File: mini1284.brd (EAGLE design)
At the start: 69.8 x 20.8 mm, 37 parts, among them U1 ATMEGA644A

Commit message: Routing looking pretty good.
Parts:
- removed C10, C11, C12, R10, R2, R3, R4, R5, R6, R7, R8, R9: (no value), _jc:M0805
- removed C13: 100nF, _jc:M0805
- removed D2: (no value), _jc:CHIPLED_1206
- removed D3: 1N4148, _jc:SOD-323F
- removed R11: 10K, _jc:M0805
- added LOGO2: OSHW_LOGO_6MILX0100-NT, ohw-logo:OSHW_6X100_NOTEXT
- C1, C2, C3, C4, C5, C9: value (none) -> 100nF
- C6: value (none) -> 10uF; device _jc:M0805 -> _jc:M1206
- C7, C8: value (none) -> 27pF
- D1: value (none) -> 1N4148; device _jc:SOD-323F -> _jc:SOD-323F-A
- L1: value (none) -> 10uH
- R1: value (none) -> 10K
- S1: device _jc:B3F-10XXOCT -> _jc:PTS810
- Y1: value (none) -> 16MHz
- moved D1 189.3 mm to (52.7, 14.3)
- moved R1 133.1 mm to (52.8, 12.1)
- moved C9 113.0 mm to (58.3, 8.10), turned to 270 degrees
- moved C7 40.9 mm to (11.3, 11.9)
- moved C8 34.7 mm to (11.3, 6.50)
- moved C6 28.2 mm to (46.8, 8.26)
- moved C5 21.8 mm to (40.4, 12.3)
- moved S1 6.08 mm to (52.9, 7.70), turned to 180 degrees
- moved C4 5.08 mm to (40.4, 7.62)
- moved JP6 5.08 mm to (62.2, 16.5)
- moved C1 5.08 mm to (19.3, 14.1)
- moved JP3 5.08 mm to (38.1, 1.27)
- moved JP4 5.08 mm to (38.1, 19.1)
- moved L1 5.08 mm to (43.2, 7.62)
- moved U1 4.45 mm to (30.5, 10.1)
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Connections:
- net /RESET: now also C9.1, D1.A, R1.1, S1.3, S1.4; no longer C13.1, D3.A, R11.1, S1.1, S1.2
- net AREF: now also C5.1; no longer C8.1
- net GND: now also S1.1, S1.2; no longer S1.3, S1.4
- net N$2: now also C8.1; no longer C6.1
- net N$3: now also C7.1; no longer C5.1
- net RST: now also C9.2; no longer C13.2
- net VCC: now also C6.1, D1.K, R1.2; no longer C7.1, D3.K, R11.2
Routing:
- net /RESET: track 99.2 -> 77.0 mm
- net VCC: track 112.8 -> 100.0 mm, vias 2 -> 1
- net N$14: track 20.6 -> 15.8 mm
- net SCK: track 37.6 -> 32.9 mm
- net N$11: track 17.4 -> 12.7 mm
- net N$9: track 20.6 -> 16.0 mm
- net N$16: track 17.3 -> 12.7 mm
- net N$15: track 20.8 -> 16.3 mm
- net N$17: track 17.5 -> 13.0 mm
- net MOSI: track 31.6 -> 27.1 mm
- net N$7: track 21.0 -> 16.5 mm
- net MISO: track 31.8 -> 27.4 mm
- net N$13: track 20.3 -> 15.9 mm
- net N$10: track 20.7 -> 16.4 mm
- net N$8: track 20.1 -> 15.9 mm
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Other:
- board size 69.8 x 20.8 mm -> 64.8 x 20.8 mm
- board text added: "0"
- board text added: "1"
- board text added: "10"
- board text added: "11"
- board text added: "12"
- board text added: "13"
- board text added: "14"
- board text added: "15"
- board text added: "16"
- board text added: "17"
- board text added: "18"
- board text added: "19"
- board text added: "2"
- board text added: "20"
- board text added: "21"
- board text added: "22"
- board text added: "23"
- board text added: "3"
- board text added: "4"
- board text added: "5"
- board text added: "6"
- board text added: "7"
- board text added: "8"
- board text added: "9"
- board text added: "A0"
- board text added: "A1"
- board text added: "A2"
- board text added: "A3"
- board text added: "A4"
- board text added: "A5"
- board text added: "A6"
- board text added: "A7"
- board text added: "BLK"
- board text added: "FTDI"
- board text added: "GRN"
- board text added: "ICSP"
- board text added: "RESET"
- board text added: "VCC"
- board text removed: "Vcc"

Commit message: Routing refinements.
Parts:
- added D2: LED, _jc:D0805A
- added LOGO1: OSHW_LOGO_8MILX0150-NT, ohw-logo:OSHW_8X150_NOTEXT
- added R2: 1K, _jc:M0805
- moved JP5 1.93 mm to (3.05, 14.5)
- moved C8 1.82 mm to (12.3, 8.03)
- moved Y1 1.44 mm to (16.0, 10.2)
- moved C7 1.08 mm to (12.3, 12.2)
- moved C1 0.51 mm to (19.8, 14.1)
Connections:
- new net N$34: D2.K, R2.2
- net GND: now also R2.1
- net SCK: now also D2.A
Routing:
- net SCK: track 32.9 -> 39.1 mm
- net N$34: track 0.00 -> 2.42 mm
- net N$3: track 18.0 -> 16.6 mm
- net N$2: track 15.0 -> 13.5 mm
- net MISO: track 27.4 -> 25.9 mm
- net MOSI: track 27.1 -> 25.8 mm
- net VCC: track 100.0 -> 101.1 mm
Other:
- board text added: "CC BY-SA"
- board text added: "Mighty Mini 1284P"
- board text added: "jc 0414 v1.0"
- board text added: "open"
- board text added: "source"

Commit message: Further tweaks.
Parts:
- U1: value ATMEGA644A -> ATmega1284P-AU
- moved LOGO1 1.27 mm to (16.1, 9.73)
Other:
- board text added: "goo.gl/5fAHca"
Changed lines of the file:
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@@
 <layer number="20" name="Dimension" color="15" fill="1" visible="yes" active="yes"/>
 <layer number="21" name="tPlace" color="7" fill="1" visible="yes" active="yes"/>
-<layer number="22" name="bPlace" color="7" fill="1" visible="yes" active="yes"/>
+<layer number="22" name="bPlace" color="7" fill="1" visible="no" active="yes"/>
 <layer number="23" name="tOrigins" color="15" fill="1" visible="yes" active="yes"/>
 <layer number="24" name="bOrigins" color="15" fill="1" visible="no" active="yes"/>
@@
 <text x="59.69" y="10.16" size="1.27" layer="22" ratio="16" rot="MR0">CC BY-SA</text>
 <text x="59.69" y="7.62" size="1.27" layer="22" ratio="16" rot="MR0">jc 0414 v1.0</text>
-<text x="13.97" y="13.716" size="1.27" layer="22" ratio="16" rot="MR0" align="center">open</text>
-<text x="13.97" y="7.366" size="1.27" layer="22" ratio="16" rot="MR0" align="center">source</text>
+<text x="13.97" y="14.986" size="1.27" layer="22" ratio="16" rot="MR0" align="center">open</text>
+<text x="13.97" y="8.636" size="1.27" layer="22" ratio="16" rot="MR0" align="center">source</text>
+<text x="13.97" y="6.096" size="1.27" layer="22" ratio="16" rot="MR0" align="center">goo.gl/5fAHca</text>
 </plain>
 <attributes>
@@
 </autorouter>
 <elements>
-<element name="U1" library="atmel" package="TQFP44" value="ATMEGA644A" x="30.48" y="10.1346" smashed="yes">
+<element name="U1" library="atmel" package="TQFP44" value="ATmega1284P-AU" x="30.48" y="10.1346" smashed="yes">
 <attribute name="OC_NEWARK" value="58M3748" x="57.149990625" y="-0.0254" size="1.778" layer="27" display="off"/>
 <attribute name="MPN" value="ATMEGA644PV-10AU" x="57.149990625" y="-0.0254" size="1.778" layer="27" display="off"/>
@@
 </element>
 <element name="LOGO2" library="ohw-logo" package="OSHW_6X100_NOTEXT" value="OSHW_LOGO_6MILX0100-NT" x="42.926" y="12.446"/>
-<element name="LOGO1" library="ohw-logo" package="OSHW_8X150_NOTEXT" value="OSHW_LOGO_8MILX0150-NT" x="16.1036" y="8.4582" rot="MR0"/>
+<element name="LOGO1" library="ohw-logo" package="OSHW_8X150_NOTEXT" value="OSHW_LOGO_8MILX0150-NT" x="16.1036" y="9.7282" rot="MR0"/>
 <element name="R2" library="_jc" package="M0805" value="1K" x="8.128" y="5.334" smashed="yes" rot="R180">
 <attribute name="NAME" x="6.374" y="6.834" size="0.8128" layer="25" ratio="16"/>

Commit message: First run sent to fab.
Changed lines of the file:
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@@
 <setting verticaltext="up"/>
 </settings>
-<grid distance="0.05" unitdist="inch" unit="inch" style="dots" multiple="1" display="yes" altdistance="0.001" altunitdist="inch" altunit="inch"/>
+<grid distance="0.05" unitdist="inch" unit="inch" style="dots" multiple="1" display="yes" altdistance="0.01" altunitdist="inch" altunit="inch"/>
 <layers>
 <layer number="1" name="Top" color="4" fill="1" visible="yes" active="yes"/>
@@
 <wire x1="1.27" y1="20.574" x2="0" y2="19.304" width="0" layer="20" curve="90"/>
 <text x="2.54" y="3.302" size="1.016" layer="21" ratio="16" rot="R180" align="center">RST</text>
-<text x="24.638" y="18.796" size="0.8128" layer="21" ratio="16">PB7:0</text>
-<text x="24.638" y="0.508" size="0.8128" layer="21" ratio="16">PD0:7</text>
-<text x="33.02" y="18.796" size="0.8128" layer="21" ratio="16">PA0:7</text>
-<text x="33.274" y="0.508" size="0.8128" layer="21" ratio="16">PC0:7</text>
+<text x="24.384" y="17.526" size="0.8128" layer="21" ratio="16">PB7:0</text>
+<text x="24.384" y="2.286" size="0.8128" layer="21" ratio="16">PD0:7</text>
+<text x="33.274" y="17.526" size="0.8128" layer="21" ratio="16">PA0:7</text>
+<text x="33.528" y="2.286" size="0.8128" layer="21" ratio="16">PC0:7</text>
 <text x="52.9082" y="5.1816" size="1.016" layer="21" ratio="16" align="center">RESET</text>
 <text x="22.86" y="17.018" size="1.016" layer="21" ratio="16" align="center">0</text>
@@
 </element>
 <element name="C1" library="_jc" package="M0805" value="100nF" x="19.812" y="14.0716" smashed="yes" rot="R90">
-<attribute name="NAME" x="18.2358" y="14.0956" size="0.8128" layer="25" ratio="16" rot="R90"/>
+<attribute name="NAME" x="21.487" y="10.5396" size="0.8128" layer="25" ratio="16" rot="R90"/>
 <attribute name="VALUE" x="22.312" y="12.5716" size="0.8128" layer="27" ratio="16" rot="R90"/>
 </element>
 <element name="C2" library="_jc" package="M0805" value="100nF" x="30.2514" y="1.4732" smashed="yes" rot="R180">
-<attribute name="NAME" x="26.6686" y="2.4398" size="0.8128" layer="25" ratio="16"/>
+<attribute name="NAME" x="33.3742" y="0.2526" size="0.8128" layer="25" ratio="16" rot="R90"/>
 <attribute name="VALUE" x="31.7514" y="3.9732" size="0.8128" layer="27" ratio="16" rot="R180"/>
 </element>
 <element name="C3" library="_jc" package="M0805" value="100nF" x="30.5308" y="18.923" smashed="yes" rot="R180">
-<attribute name="NAME" x="26.7956" y="17.248" size="0.8128" layer="25" ratio="16"/>
+<attribute name="NAME" x="28.218" y="18.9216" size="0.8128" layer="25" ratio="16" rot="R90"/>
 <attribute name="VALUE" x="32.0308" y="21.423" size="0.8128" layer="27" ratio="16" rot="R180"/>
 </element>
@@
 <via x="43.18" y="11.43" extent="1-16" drill="0.6"/>
 <contactref element="R2" pad="1"/>
-<via x="26.67" y="19.05" extent="1-16" drill="0.4064"/>
+<via x="25.4" y="19.05" extent="1-16" drill="0.4064"/>
 <via x="26.67" y="12.7" extent="1-16" drill="0.4064"/>
 <via x="55.88" y="12.065" extent="1-16" drill="0.4064"/>

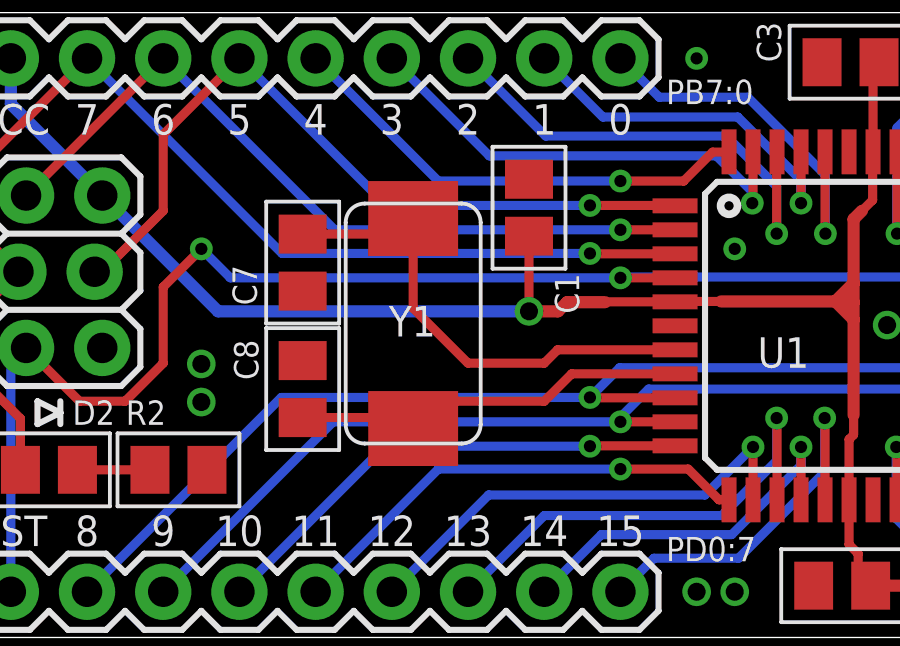
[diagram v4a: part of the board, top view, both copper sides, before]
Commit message: Change to Epson crystal.
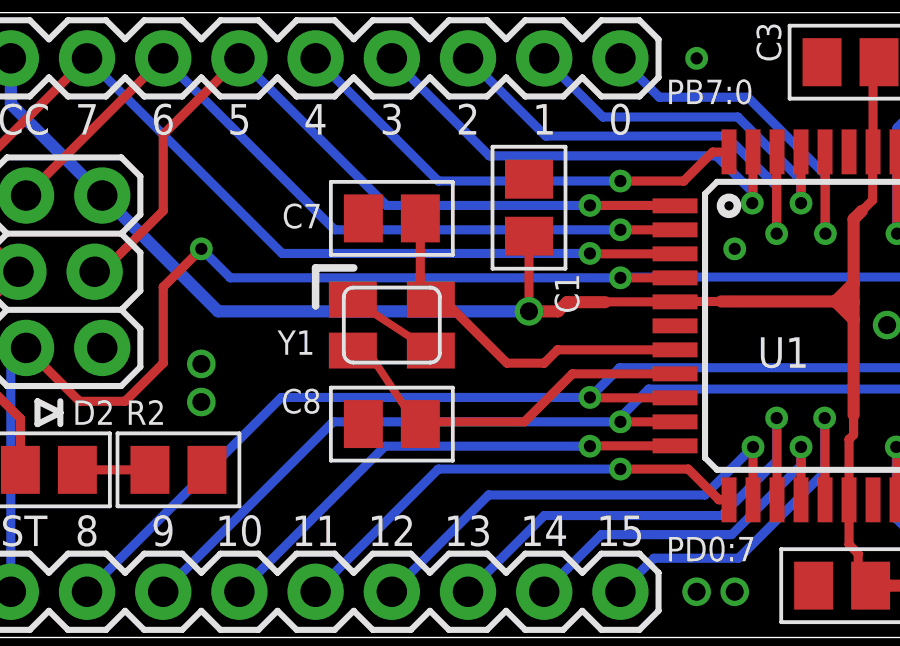
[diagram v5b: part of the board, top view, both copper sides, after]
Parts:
- Y1: value 16MHz -> (none); device _jc:CRYSTAL-ABRACON-ABM2 -> _jc:CRYSTAL-EPSON-TSX3225
- moved C7 3.32 mm to (15.2, 13.7), turned to 180 degrees
- moved C8 3.19 mm to (15.2, 6.86), turned to 180 degrees
- moved Y1 0.71 mm to (15.2, 10.2), turned to 180 degrees
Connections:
- net GND: now also Y1.2, Y1.4
- net N$2: now also Y1.3; no longer Y1.P$2
- net N$3: now also Y1.1; no longer Y1.P$1
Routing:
- net N$3: track 16.6 -> 12.1 mm
- net GND: track 0.00 -> 3.11 mm
- net N$2: track 13.5 -> 12.7 mm
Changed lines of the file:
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@@
 <setting verticaltext="up"/>
 </settings>
-<grid distance="0.05" unitdist="inch" unit="inch" style="dots" multiple="1" display="yes" altdistance="0.01" altunitdist="inch" altunit="inch"/>
+<grid distance="0.05" unitdist="inch" unit="inch" style="dots" multiple="1" display="yes" altdistance="0.001" altunitdist="inch" altunit="inch"/>
 <layers>
 <layer number="1" name="Top" color="4" fill="1" visible="yes" active="yes"/>
@@
 <attribute name="VALUE" x="37.9368" y="9.12" size="0.8128" layer="27" ratio="16" rot="R270"/>
 </element>
-<element name="C7" library="_jc" package="M0805" value="27pF" x="12.2682" y="12.2428" smashed="yes" rot="R270">
-<attribute name="NAME" x="10.7428" y="10.819" size="0.8128" layer="25" ratio="16" rot="R90"/>
-<attribute name="VALUE" x="9.7682" y="13.7428" size="0.8128" layer="27" ratio="16" rot="R270"/>
-</element>
-<element name="C8" library="_jc" package="M0805" value="27pF" x="12.2682" y="8.0264" smashed="yes" rot="R90">
-<attribute name="NAME" x="10.7936" y="8.3298" size="0.8128" layer="25" ratio="16" rot="R90"/>
-<attribute name="VALUE" x="14.7682" y="6.5264" size="0.8128" layer="27" ratio="16" rot="R90"/>
+<element name="C7" library="_jc" package="M0805" value="27pF" x="15.24" y="13.716" smashed="yes" rot="R180">
+<attribute name="NAME" x="11.581" y="13.3872" size="0.8128" layer="25" ratio="16"/>
+<attribute name="VALUE" x="16.74" y="16.216" size="0.8128" layer="27" ratio="16" rot="R180"/>
+</element>
+<element name="C8" library="_jc" package="M0805" value="27pF" x="15.24" y="6.858" smashed="yes" rot="R180">
+<attribute name="NAME" x="11.5556" y="7.215" size="0.8128" layer="25" ratio="16"/>
+<attribute name="VALUE" x="16.74" y="9.358" size="0.8128" layer="27" ratio="16" rot="R180"/>
 </element>
 <element name="C6" library="_jc" package="M1206" value="10uF" x="46.7614" y="8.255" smashed="yes" rot="R270">
@@
 <element name="JP4" library="SparkFun" package="1X09" value="M09" x="38.1" y="19.05" smashed="yes">
 <attribute name="VALUE" x="36.83" y="15.875" size="1.27" layer="27"/>
-</element>
-<element name="Y1" library="_jc" package="CRYSTAL-ABRACON-ABM2" value="16MHz" x="15.9512" y="10.2108" smashed="yes" rot="R270">
-<attribute name="NAME" x="15.1384" y="9.779" size="1.016" layer="25" ratio="16"/>
-<attribute name="VALUE" x="12.1412" y="11.4808" size="1.016" layer="27" ratio="16" rot="R270"/>
 </element>
 <element name="JP5" library="_jc" package="2X3_LOCK" value="ICSP" x="3.048" y="14.478" smashed="yes" rot="R270">
@@
 <attribute name="NAME" x="4.596" y="6.834" size="0.8128" layer="25" ratio="16"/>
 <attribute name="VALUE" x="2.31" y="2.834" size="0.8128" layer="27" ratio="16"/>
+</element>
+<element name="Y1" library="_jc" package="CRYSTAL-EPSON-TSX3225" value="" x="15.24" y="10.16" smashed="yes" rot="R180">
+<attribute name="NAME" x="11.43" y="9.1694" size="0.8128" layer="25" ratio="16"/>
+<attribute name="VALUE" x="16.51" y="12.7" size="0.8128" layer="27" ratio="16" rot="R180"/>
 </element>
 </elements>
@@
 <via x="26.67" y="12.7" extent="1-16" drill="0.4064"/>
 <via x="55.88" y="12.065" extent="1-16" drill="0.4064"/>
+<contactref element="Y1" pad="4"/>
+<contactref element="Y1" pad="2"/>
+<wire x1="13.94" y1="11.01" x2="16.54" y2="9.31" width="0.254" layer="1"/>
 </signal>
 <signal name="RST">
@@
 <contactref element="U1" pad="8"/>
 <contactref element="C8" pad="1"/>
-<contactref element="Y1" pad="P$2"/>
-<wire x1="24.68" y1="8.5346" x2="21.2346" y2="8.5346" width="0.3048" layer="1"/>
-<wire x1="21.2346" y1="8.5346" x2="20.32" y2="7.62" width="0.3048" layer="1"/>
-<wire x1="20.32" y1="7.62" x2="16.51" y2="7.62" width="0.3048" layer="1"/>
-<wire x1="16.51" y1="7.62" x2="16.51" y2="7.2696" width="0.3048" layer="1"/>
-<wire x1="16.51" y1="7.2696" x2="15.9512" y2="6.7108" width="0.3048" layer="1"/>
-<wire x1="12.2682" y1="7.0764" x2="15.5856" y2="7.0764" width="0.3048" layer="1"/>
-<wire x1="15.5856" y1="7.0764" x2="15.9512" y2="6.7108" width="0.3048" layer="1"/>
+<contactref element="Y1" pad="3"/>
+<wire x1="14.5034" y1="9.1948" x2="13.94" y2="9.31" width="0.254" layer="1"/>
+<wire x1="14.5034" y1="9.1948" x2="15.7988" y2="7.239" width="0.254" layer="1"/>
+<wire x1="15.7988" y1="7.239" x2="16.19" y2="6.858" width="0.254" layer="1"/>
+<wire x1="24.68" y1="8.5346" x2="21.26" y2="8.5346" width="0.3048" layer="1"/>
+<wire x1="21.26" y1="8.5346" x2="19.6596" y2="6.9342" width="0.3048" layer="1"/>
+<wire x1="19.6596" y1="6.9342" x2="16.2662" y2="6.9342" width="0.3048" layer="1"/>
+<wire x1="16.2662" y1="6.9342" x2="16.19" y2="6.858" width="0.3048" layer="1"/>
 </signal>
 <signal name="N$3">
 <contactref element="U1" pad="7"/>
 <contactref element="C7" pad="1"/>
-<contactref element="Y1" pad="P$1"/>
+<contactref element="Y1" pad="1"/>
 <wire x1="24.68" y1="9.3346" x2="20.7646" y2="9.3346" width="0.3048" layer="1"/>
 <wire x1="20.7646" y1="9.3346" x2="20.32" y2="8.89" width="0.3048" layer="1"/>
-<wire x1="20.32" y1="8.89" x2="17.78" y2="8.89" width="0.3048" layer="1"/>
-<wire x1="17.78" y1="8.89" x2="15.9512" y2="10.7188" width="0.3048" layer="1"/>
-<wire x1="15.9512" y1="10.7188" x2="15.9512" y2="13.7108" width="0.3048" layer="1"/>
-<wire x1="12.2682" y1="13.1928" x2="15.4332" y2="13.1928" width="0.3048" layer="1"/>
-<wire x1="15.4332" y1="13.1928" x2="15.9512" y2="13.7108" width="0.3048" layer="1"/>
+<wire x1="20.32" y1="8.89" x2="19.0754" y2="8.89" width="0.3048" layer="1"/>
+<wire x1="19.0754" y1="8.89" x2="17.2466" y2="10.7188" width="0.3048" layer="1"/>
+<wire x1="17.2466" y1="10.7188" x2="16.8312" y2="10.7188" width="0.3048" layer="1"/>
+<wire x1="16.8312" y1="10.7188" x2="16.54" y2="11.01" width="0.3048" layer="1"/>
+<wire x1="16.19" y1="13.716" x2="16.19" y2="11.36" width="0.3048" layer="1"/>
+<wire x1="16.19" y1="11.36" x2="16.54" y2="11.01" width="0.3048" layer="1"/>
 </signal>
 <signal name="AREF">
